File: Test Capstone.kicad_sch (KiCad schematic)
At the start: 4 parts, among them U1 SCD30

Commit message: october nine
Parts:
- added IC1: 1085, 1085, symbol 1085:1085
- added RSCL, RSDA: R, symbol Device:R
- U1: Value_1 SCD30 -> SCD30_CO2
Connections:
- net 3V3: now also NO2-ULPSM_1.7 (Vsupply(3.3V)), NO2-ULPSM_1.8 (Vsupply(3.3V))
- net 5V: now also RSCL.1, RSDA.1
- net GND: now also NO2-ULPSM_1.6 (GND)
- net SDA: now reaches A1.A4(SDA) (AD4/SDA)
- net SDA: now also PM_SNGCJA1.2 (SDA), U1.4 (RX/_SDA), IC1.7 (SDA), RSDA.2
- net SCL: now reaches A1.A5(SCL) (AD5/SCL)
- net SCL: now also PM_SNGCJA1.3 (SCL), U1.3 (TX/_SCL), IC1.8 (SCL), RSCL.2
- net ADC1: now reaches NO2-ULPSM_1.1 (Vgas)
- net ADC1: now also IC1.3 (A1)
- net A0: no longer names the net of A1.A0
- net A0: no longer U1.4 (RX/_SDA)
- net A1: no longer names the net of A1.A1
- net A1: no longer U1.3 (TX/_SCL)
- net A2: no longer names the net of A1.A2
- net A2: no longer PM_SNGCJA1.2 (SDA)
- net A3: no longer names the net of A1.A3
- net A3: no longer PM_SNGCJA1.3 (SCL)
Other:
- note added: "ANALOG TO DIGITAL CONVERTER"
- note added: "ARDUINO CIRCUITRY"
- note added: "CO2 SENSOR"
- note added: "I2C SETUP"
- note added: "NO2 SENSOR"
- note added: "PM SENSOR"
- moved on the sheet: A1A, A1B, A1C, A1D, NO2-ULPSM_1, PM_SNGCJA1, U1

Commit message: sch edits
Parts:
- added CO-ULPSM_1, SO2-ULPSM_1: ~, symbol Capstone Library:NO2
- added IC2: 1085, 1085, symbol 1085:1085
- added R1, R2, R3, R4, R5, R6: 10K, symbol Device:R
- renumbered RSCL to RSCL1, RSDA to RSDA1
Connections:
- net 3V3: now also CO-ULPSM_1.8 (Vsupply(3.3V)), R2.2, R4.2, R6.2, SO2-ULPSM_1.8 (Vsupply(3.3V)); no longer NO2-ULPSM_1.7 (Vsupply(3.3V))
- net GND: now also CO-ULPSM_1.6 (GND), R1.1, R3.1, R5.1, SO2-ULPSM_1.6 (GND)
- net SCL: now also IC2.8 (SCL)
- net SDA: now also IC2.7 (SDA)
- net ADC0: now reaches IC1.4 (A0)
- net ADC0: now also NO2-ULPSM_1.3 (Vtemp)
- net at NO2-ULPSM_1.2 (Vref): now also R1.2, R2.1
- new net: R3.2, R4.1, SO2-ULPSM_1.2 (Vref)
- new net: CO-ULPSM_1.2 (Vref), R5.2, R6.1
- new net ADC2: SO2-ULPSM_1.3 (Vtemp)
- new net ADC3: SO2-ULPSM_1.1 (Vgas)
- new net ADC4: CO-ULPSM_1.3 (Vtemp), IC2.4 (A0)
- new net ADC5: CO-ULPSM_1.1 (Vgas), IC2.3 (A1)
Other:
- note added: "CO SENSOR"
- note added: "SO2 SENSOR"
- moved on the sheet: IC1, NO2-ULPSM_1

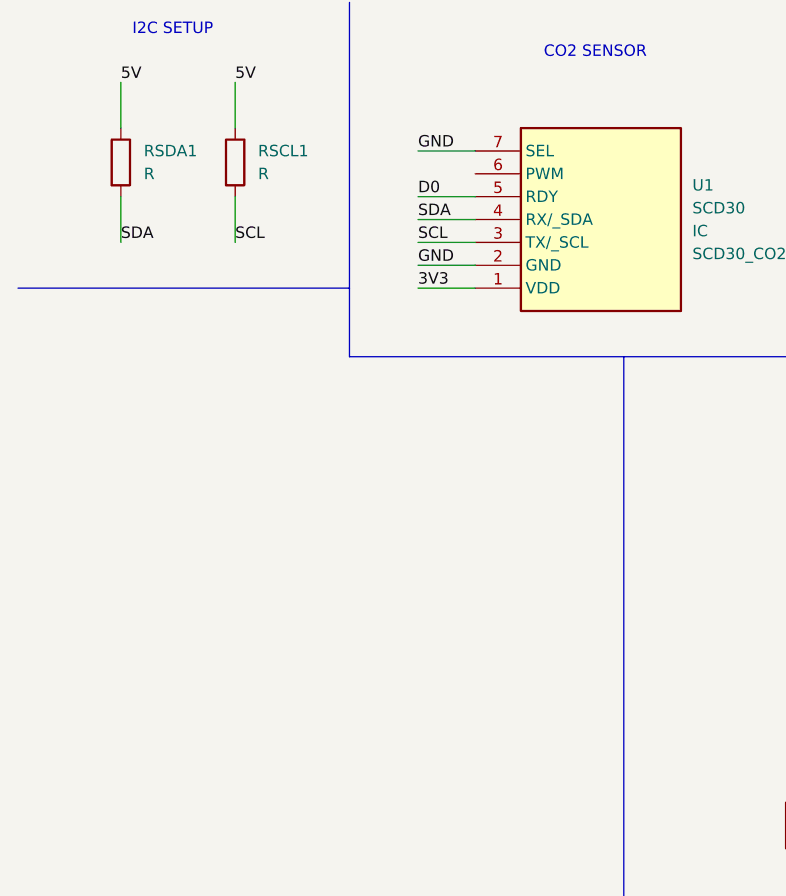
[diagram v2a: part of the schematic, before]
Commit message: added scd30 file
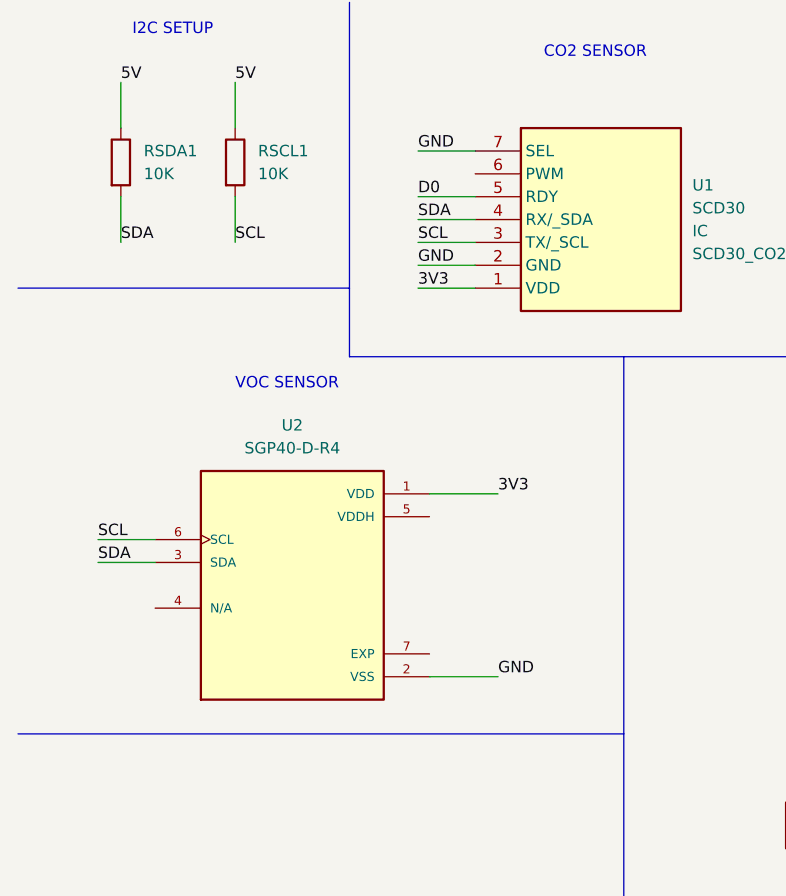
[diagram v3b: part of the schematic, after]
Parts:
- added U2: SGP40-D-R4, SGP40-D-R4:XCDR_SGP40-D-R4, symbol Capstone Library:SGP40-D-R4
- RSCL1, RSDA1: value R -> 10K
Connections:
- net 3V3: now also U2.1 (VDD)
- net GND: now also U2.2 (VSS)
- net SCL: now also U2.6 (SCL)
- net SDA: now also U2.3 (SDA)
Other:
- note added: "VOC SENSOR"
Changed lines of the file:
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@@
+    (stroke (width 0) (type default))
+  )
+  (wire (pts (xy 20.32 73.66) (xy 26.67 73.66))
     (stroke (width 0) (type default))
   )
@@
     (stroke (width 0) (type default))
   )
+  (polyline (pts (xy 11.43 92.71) (xy 78.74 92.71))
+    (stroke (width 0) (type default))
+  )
+  (wire (pts (xy 57.15 66.04) (xy 64.77 66.04))
+    (stroke (width 0) (type default))
+  )
   (wire (pts (xy 146.05 54.61) (xy 152.4 54.61))
     (stroke (width 0) (type default))
@@
     (stroke (width 0) (type default))
   )
+  (wire (pts (xy 20.32 71.12) (xy 26.67 71.12))
+    (stroke (width 0) (type default))
+  )
   (wire (pts (xy 116.84 170.18) (xy 123.19 170.18))
     (stroke (width 0) (type default))
@@
     (stroke (width 0) (type default))
   )
+  (wire (pts (xy 57.15 86.36) (xy 64.77 86.36))
+    (stroke (width 0) (type default))
+  )
   (polyline (pts (xy 101.6 71.12) (xy 181.61 71.12))
     (stroke (width 0) (type default))
@@
     (effects (font (size 1.27 1.27)) (justify left bottom))
   )
+  (text "VOC SENSOR" (at 35.56 54.61 0)
+    (effects (font (size 1.27 1.27)) (justify left bottom))
+  )
   (text "PM SENSOR" (at 255.27 115.57 0)
     (effects (font (size 1.27 1.27)) (justify left bottom))
@@
     (effects (font (size 1.27 1.27)) (justify left bottom))
   )
+  (label "SCL" (at 20.32 71.12 0) (fields_autoplaced)
+    (effects (font (size 1.27 1.27)) (justify left bottom))
+  )
   (label "3V3" (at 92.71 125.73 0) (fields_autoplaced)
     (effects (font (size 1.27 1.27)) (justify left bottom))
@@
     (effects (font (size 1.27 1.27)) (justify left bottom))
   )
+  (label "SDA" (at 20.32 73.66 0) (fields_autoplaced)
+    (effects (font (size 1.27 1.27)) (justify left bottom))
+  )
   (label "D0" (at 55.88 33.02 0) (fields_autoplaced)
     (effects (font (size 1.27 1.27)) (justify left bottom))
@@
     (effects (font (size 1.27 1.27)) (justify left bottom))
   )
+  (label "GND" (at 64.77 86.36 0) (fields_autoplaced)
+    (effects (font (size 1.27 1.27)) (justify left bottom))
+  )
   (label "SCL" (at 35.56 38.1 0) (fields_autoplaced)
     (effects (font (size 1.27 1.27)) (justify left bottom))
@@
   )
   (label "GND" (at 55.88 40.64 0) (fields_autoplaced)
+    (effects (font (size 1.27 1.27)) (justify left bottom))
+  )
+  (label "3V3" (at 64.77 66.04 0) (fields_autoplaced)
     (effects (font (size 1.27 1.27)) (justify left bottom))
   )
@@
     )
   )
+  (symbol (lib_id "Capstone Library:SGP40-D-R4") (at 41.91 76.2 0) (unit 1)
+    (in_bom yes) (on_board yes) (dnp no) (fields_autoplaced)
+    (property "Reference" "U2" (at 41.91 58.42 0)
+      (effects (font (size 1.27 1.27)))
+    )
+    (property "Value" "SGP40-D-R4" (at 41.91 60.96 0)
+      (effects (font (size 1.27 1.27)))
+    )
+    (property "Footprint" "SGP40-D-R4:XCDR_SGP40-D-R4" (at 41.91 76.2 0)
+      (effects (font (size 1.27 1.27)) (justify bottom) hide)
+    )
+    (property "Datasheet" "" (at 41.91 76.2 0)
+      (effects (font (size 1.27 1.27)) hide)
+    )
+    (property "MF" "Sensirion AG" (at 41.91 76.2 0)
+      (effects (font (size 1.27 1.27)) (justify bottom) hide)
+    )
+    (property "MAXIMUM_PACKAGE_HEIGHT" "0.95mm" (at 41.91 76.2 0)
+      (effects (font (size 1.27 1.27)) (justify bottom) hide)
+    )
+    (property "Package" "None" (at 41.91 76.2 0)
+      (effects (font (size 1.27 1.27)) (justify bottom) hide)
+    )
+    (property "Price" "None" (at 41.91 76.2 0)
+      (effects (font (size 1.27 1.27)) (justify bottom) hide)
+    )
+    (property "Check_prices" "https://www.snapeda.com/parts/SGP40-D-R4/Sensirion+AG/view-part/?ref=eda" (at 41.91 76.2 0)
+      (effects (font (size 1.27 1.27)) (justify bottom) hide)
+    )
+    (property "STANDARD" "Manufacturer Recommendations" (at 41.91 76.2 0)
+      (effects (font (size 1.27 1.27)) (justify bottom) hide)
+    )
+    (property "PARTREV" "1.2" (at 41.91 76.2 0)
+      (effects (font (size 1.27 1.27)) (justify bottom) hide)
+    )
+    (property "SnapEDA_Link" "https://www.snapeda.com/parts/SGP40-D-R4/Sensirion+AG/view-part/?ref=snap" (at 41.91 76.2 0)
+      (effects (font (size 1.27 1.27)) (justify bottom) hide)
+    )
+    (property "MP" "SGP40-D-R4" (at 41.91 76.2 0)
+      (effects (font (size 1.27 1.27)) (justify bottom) hide)
+    )
+    (property "Purchase-URL" "https://www.snapeda.com/api/url_track_click_mouser/?unipart_id=5003465&manufacturer=Sensirion AG&part_name=SGP40-D-R4&search_term=None" (at 41.91 76.2 0)
+      (effects (font (size 1.27 1.27)) (justify bottom) hide)
+    )
+    (property "Description" "\nAIR QUALITY GAS SENSOR LOW POWER\n" (at 41.91 76.2 0)
+      (effects (font (size 1.27 1.27)) (justify bottom) hide)
+    )
+    (property "MANUFACTURER" "Sensirion AG" (at 41.91 76.2 0)
+      (effects (font (size 1.27 1.27)) (justify bottom) hide)
+    )
+    (property "Availability" "In Stock" (at 41.91 76.2 0)
+      (effects (font (size 1.27 1.27)) (justify bottom) hide)
+    )
+    (property "SNAPEDA_PN" "SGP40-D-R4" (at 41.91 76.2 0)
+      (effects (font (size 1.27 1.27)) (justify bottom) hide)
+    )
+    (pin "1")
+    (pin "2")
+    (pin "3")
+    (pin "4")
+    (pin "5")
+    (pin "6")
+    (pin "7")
+    (instances
+      (project "Test Capstone"
+        (path "/fca1b5fd-bc33-4f10-9462-8a8bf71c35e9"
+          (reference "U2") (unit 1)
+        )
+      )
+    )
+  )
   (symbol (lib_id "A000066:A000066") (at 260.35 76.2 0) (unit 4)
     (in_bom yes) (on_board yes) (dnp no) (fields_autoplaced)
@@
       (effects (font (size 1.27 1.27)) (justify left))
     )
-    (property "Value" "R" (at 25.4 30.48 0)
+    (property "Value" "10K" (at 25.4 30.48 0)
       (effects (font (size 1.27 1.27)) (justify left))
     )
@@
       (effects (font (size 1.27 1.27)) (justify left))
     )
-    (property "Value" "R" (at 38.1 30.48 0)
-      (effects (font (size 1.27 1.27)) (justify left))
-    )
+    (property "Value" "10K" (at 38.1 30.48 0)
+      (effects (font (size 1.27 1.27)) (justify left))
+    )

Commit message: schematic edits small cdr2
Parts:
- RSCL1, RSDA1: value 10K -> 4.7K
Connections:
- net 5V: now also IC1.10 (VDD), IC2.10 (VDD)
- net ADC2: now also IC1.2 (A2)
- net ADC3: now also IC1.1 (A3)
- net GND: now also IC1.9 (GND), IC2.9 (GND)
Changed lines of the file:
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@@
+    (stroke (width 0) (type default))
+  )
+  (wire (pts (xy 105.41 40.64) (xy 111.76 40.64))
     (stroke (width 0) (type default))
   )
@@
     (stroke (width 0) (type default))
   )
+  (wire (pts (xy 146.05 39.37) (xy 152.4 39.37))
+    (stroke (width 0) (type default))
+  )
   (wire (pts (xy 105.41 55.88) (xy 111.76 55.88))
     (stroke (width 0) (type default))
@@
     (stroke (width 0) (type default))
   )
+  (wire (pts (xy 105.41 60.96) (xy 111.76 60.96))
+    (stroke (width 0) (type default))
+  )
   (wire (pts (xy 242.57 138.43) (xy 254 138.43))
     (stroke (width 0) (type default))
@@
     (stroke (width 0) (type default))
   )
+  (wire (pts (xy 105.41 38.1) (xy 111.76 38.1))
+    (stroke (width 0) (type default))
+  )
   (wire (pts (xy 97.79 106.68) (xy 97.79 110.49))
     (stroke (width 0) (type default))
@@
     (stroke (width 0) (type default))
   )
+  (wire (pts (xy 146.05 41.91) (xy 152.4 41.91))
+    (stroke (width 0) (type default))
+  )
   (polyline (pts (xy 11.43 43.18) (xy 48.26 43.18))
     (stroke (width 0) (type default))
@@
     (stroke (width 0) (type default))
   )
+  (wire (pts (xy 105.41 58.42) (xy 111.76 58.42))
+    (stroke (width 0) (type default))
+  )
   (wire (pts (xy 101.6 173.99) (xy 101.6 177.8))
     (stroke (width 0) (type default))
@@
     (effects (font (size 1.27 1.27)) (justify left bottom))
   )
+  (label "GND" (at 146.05 41.91 0) (fields_autoplaced)
+    (effects (font (size 1.27 1.27)) (justify left bottom))
+  )
   (label "GND" (at 172.72 107.95 0) (fields_autoplaced)
     (effects (font (size 1.27 1.27)) (justify left bottom))
@@
     (effects (font (size 1.27 1.27)) (justify left bottom))
   )
+  (label "5V" (at 146.05 39.37 0) (fields_autoplaced)
+    (effects (font (size 1.27 1.27)) (justify left bottom))
+  )
   (label "3V3" (at 55.88 43.18 0) (fields_autoplaced)
     (effects (font (size 1.27 1.27)) (justify left bottom))
@@
     (effects (font (size 1.27 1.27)) (justify left bottom))
   )
+  (label "ADC3" (at 105.41 60.96 0) (fields_autoplaced)
+    (effects (font (size 1.27 1.27)) (justify left bottom))
+  )
   (label "SCL" (at 242.57 134.62 0) (fields_autoplaced)
     (effects (font (size 1.27 1.27)) (justify left bottom))
@@
     (effects (font (size 1.27 1.27)) (justify left bottom))
   )
+  (label "5V" (at 105.41 38.1 0) (fields_autoplaced)
+    (effects (font (size 1.27 1.27)) (justify left bottom))
+  )
   (label "5V" (at 242.57 142.24 0) (fields_autoplaced)
     (effects (font (size 1.27 1.27)) (justify left bottom))
@@
     (effects (font (size 1.27 1.27)) (justify left bottom))
   )
+  (label "ADC2" (at 105.41 58.42 0) (fields_autoplaced)
+    (effects (font (size 1.27 1.27)) (justify left bottom))
+  )
   (label "ADC4" (at 116.84 170.18 0) (fields_autoplaced)
     (effects (font (size 1.27 1.27)) (justify left bottom))
   )
   (label "5V" (at 22.86 20.32 0) (fields_autoplaced)
+    (effects (font (size 1.27 1.27)) (justify left bottom))
+  )
+  (label "GND" (at 105.41 40.64 0) (fields_autoplaced)
     (effects (font (size 1.27 1.27)) (justify left bottom))
   )
@@
       (effects (font (size 1.27 1.27)) (justify left))
     )
-    (property "Value" "10K" (at 25.4 30.48 0)
+    (property "Value" "4.7K" (at 25.4 30.48 0)
       (effects (font (size 1.27 1.27)) (justify left))
     )
@@
       (effects (font (size 1.27 1.27)) (justify left))
     )
-    (property "Value" "10K" (at 38.1 30.48 0)
-      (effects (font (size 1.27 1.27)) (justify left))
-    )
+    (property "Value" "4.7K" (at 38.1 30.48 0)
+      (effects (font (size 1.27 1.27)) (justify left))
+    )
